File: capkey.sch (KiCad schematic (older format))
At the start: 19 parts, among them J1 TIP, J2 RING, J3 AudioJack4, Q1 Q_NMOS_DGS, Q2 Q_NMOS_DGS, SW1 SW_SPDT, U1 AT42QT1011-TSHR, U2 AT42QT1011-TSHR, U3 L78L05_SOT89

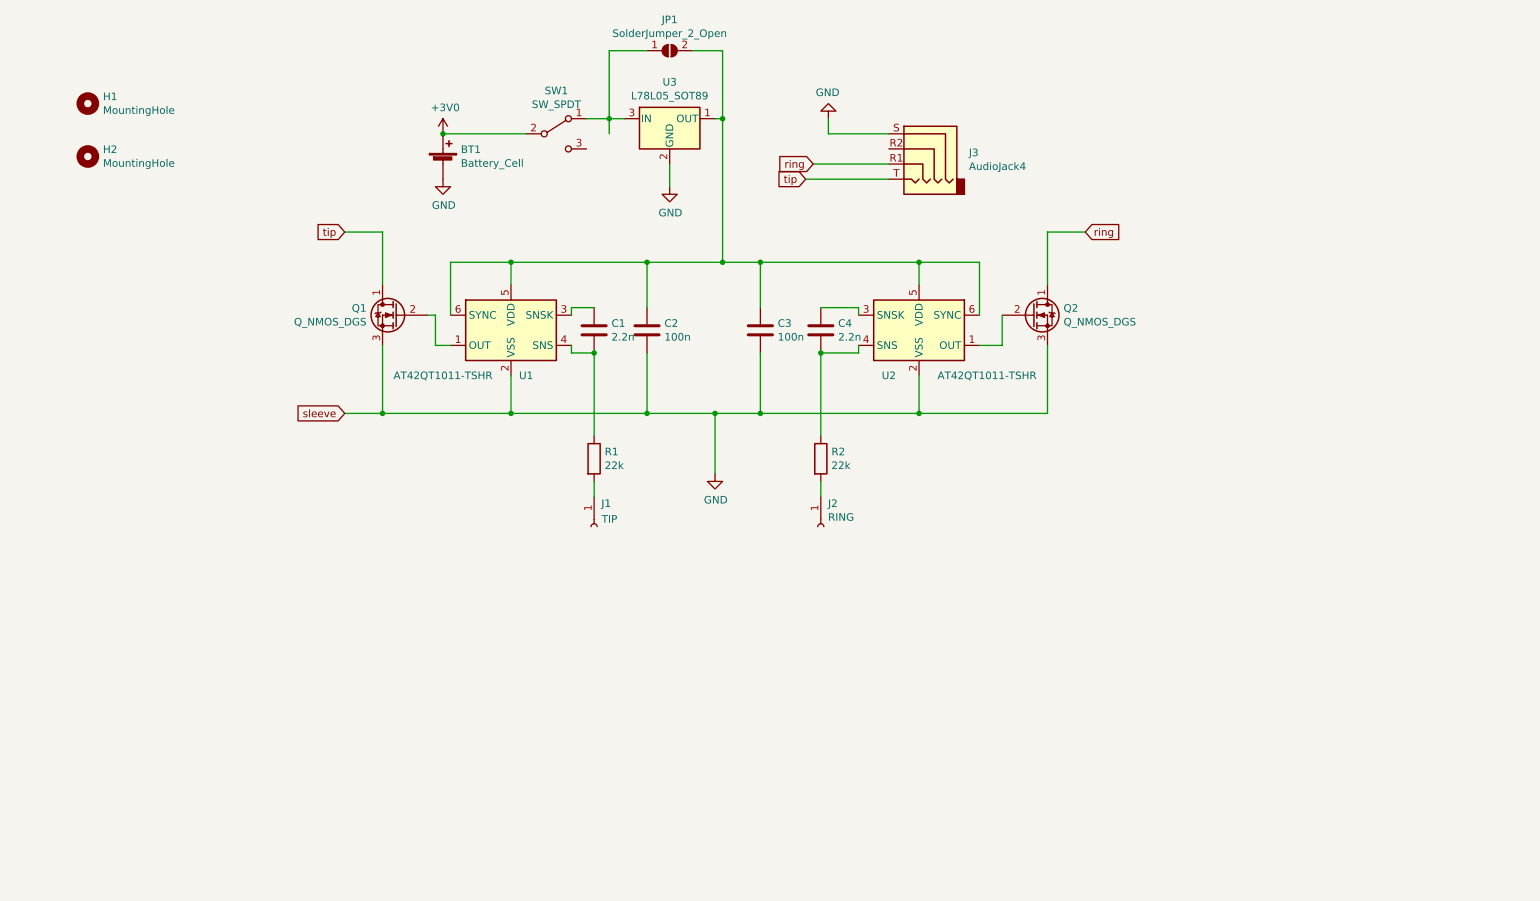
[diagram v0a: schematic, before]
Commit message: Added attiny keyer
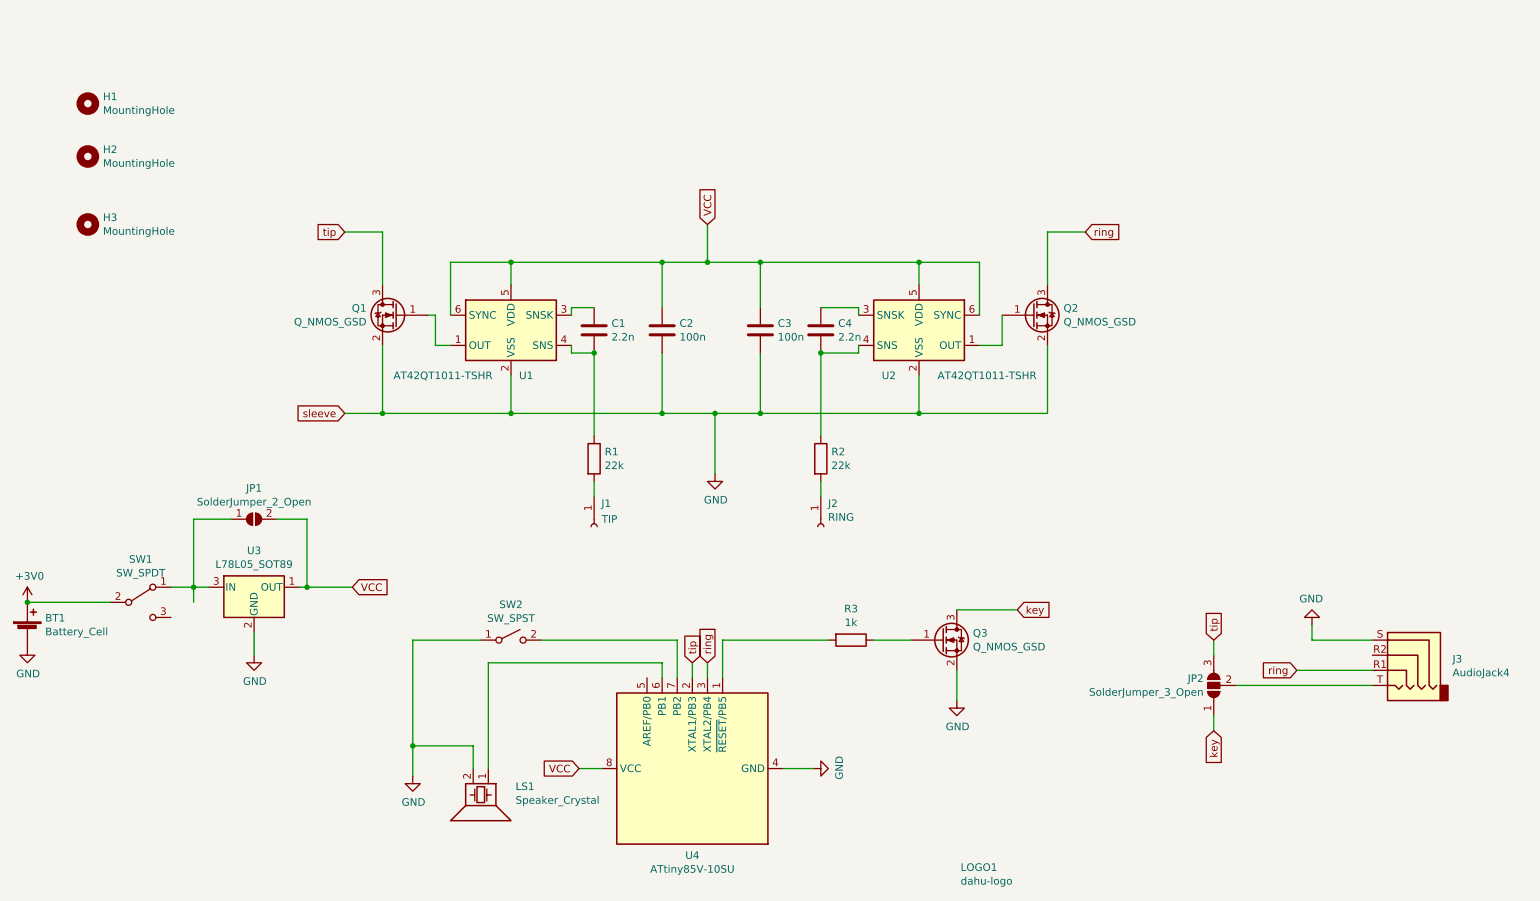
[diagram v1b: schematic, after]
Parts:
- removed Q1, Q2: Q_NMOS_DGS, Package_TO_SOT_SMD:SOT-23, symbol Device:Q_NMOS_DGS
- added H3: MountingHole, MountingHole:MountingHole_2.1mm, symbol Mechanical:MountingHole
- added JP2: SolderJumper_3_Open, Jumper:SolderJumper-3_P1.3mm_Open_RoundedPad1.0x1.5mm, symbol Jumper:SolderJumper_3_Open
- added LOGO1: dahu-logo, w6ipa-footprints:W6IPA-Logo-9mmx8mm, symbol w6ipa_graphic:dahu-logo
- added LS1: Speaker_Crystal, w6ipa-footprints:CPT-9019S-SMT-TR, symbol Device:Speaker_Crystal
- added Q1, Q2, Q3: Q_NMOS_GSD, Package_TO_SOT_SMD:SOT-23, symbol Device:Q_NMOS_GSD
- added R3: 1k, Resistor_SMD:R_0805_2012Metric, symbol Device:R
- added SW2: SW_SPST, w6ipa-footprints:SW_Push_1P1T_NO_CK_PTS647, symbol Switch:SW_SPST
- added U4: ATtiny85V-10SU, Package_SO:SOIJ-8_5.3x5.3mm_P1.27mm, symbol MCU_Microchip_ATtiny:ATtiny85V-10SU
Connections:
- net GND: now also LS1.2, Q1.2 (S), Q2.2 (S), Q3.2 (S), SW2.1 (A), U4.4 (GND)
- net ring: now also Q2.3 (D), U4.3 (XTAL2/PB4)
- net tip: now also JP2.3 (B), Q1.3 (D), U4.2 (XTAL1/PB3); no longer J3.T
- net at U2.1 (OUT): now also Q2.1 (G)
- net VCC: now reaches C2.1, C3.1, JP1.2 (B), U1.5 (VDD), U1.6 (SYNC), U2.5 (VDD), U2.6 (SYNC), U3.1 (OUT)
- net VCC: now also U4.8 (VCC)
- net at U1.1 (OUT): now also Q1.1 (G)
- new net: J3.T, JP2.2 (C)
- new net: R3.2, U4.1 (~RESET~/PB5)
- new net: LS1.1, U4.6 (PB1)
- new net: SW2.2 (B), U4.7 (PB2)
- new net: Q3.1 (G), R3.1
- new net key: JP2.1 (A), Q3.3 (D)
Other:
- moved on the sheet: BT1, C2, J3, JP1, SW1, U3

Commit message: 7805 -> 7833
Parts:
- U3: value L78L05_SOT89 -> L78L33_SOT89; symbol Regulator_Linear:L78L05_SOT89 -> Regulator_Linear:L78L33_SOT89
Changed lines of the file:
@@
 EESchema Schematic File Version 4
+LIBS:capkey-cache
 EELAYER 30 0
 EELAYER END
@@
 $EndComp
 $Comp
-L Regulator_Linear:L78L05_SOT89 U3
+L Regulator_Linear:L78L33_SOT89 U3
 U 1 1 5E3EEBE6
 P 2650 4950
 F 0 "U3" H 2650 5192 50  0000 C CNN
-F 1 "L78L05_SOT89" H 2650 5101 50  0000 C CNN
+F 1 "L78L33_SOT89" H 2650 5101 50  0000 C CNN
 F 2 "Package_TO_SOT_SMD:SOT-89-3" H 2650 5150 50  0001 C CIN
 F 3 "http://www.st.com/content/ccc/resource/technical/document/datasheet/15/55/e5/aa/23/5b/43/fd/CD00000446.pdf/files/CD00000446.pdf/jcr:content/translations/en.CD00000446.pdf" H 2650 4900 50  0001 C CNN
